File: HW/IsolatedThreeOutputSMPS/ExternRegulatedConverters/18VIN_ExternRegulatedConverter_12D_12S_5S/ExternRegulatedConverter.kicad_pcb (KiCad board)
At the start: 2 copper layers, 71.1 x 47 mm, 20 parts, among them J1 15VDC, J2 Conn_01x07, U1 RS6-1212D, U2 LM7805_TO220, U3 LM7812_TO220, U4 LM7912_TO220, U5 LM7812_TO220

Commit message: RevA layout PSU
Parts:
- added C10: 100nF, Capacitor_SMD:C_0805_2012Metric_Pad1.15x1.40mm_HandSolder, F.Cu at (104.9, 114.3)
- added C13: 1uF, Capacitor_SMD:CP_Elec_4x5.7, F.Cu at (154.2, 108.0)
- added C14: 4.7uF, Capacitor_SMD:CP_Elec_4x5.7, F.Cu at (150.4, 85.0)
- added D2: ES2G, Diode_SMD:D_SMA_Handsoldering, F.Cu at (154.2, 100.3)
- added HS2: Heatsink, Heatsink:Heatsink_SheetType_50x7mm_2Fixations, B.Cu at (108.0, 97.8)
- added REF**: MountingHole_3.2mm_M3_DIN965, MountingHole:MountingHole_3.2mm_M3_DIN965, F.Cu at (108.0, 91.1)
- added REF**: MountingHole_3.2mm_M3_DIN965, MountingHole:MountingHole_3.2mm_M3_DIN965, F.Cu at (108.0, 107.6)
- added REF**: MountingHole_3.2mm_M3_DIN965, MountingHole:MountingHole_3.2mm_M3_DIN965, F.Cu at (147.3, 91.1)
- added REF**: MountingHole_3.2mm_M3_DIN965, MountingHole:MountingHole_3.2mm_M3_DIN965, F.Cu at (147.3, 107.6)
- added REF**: MountingHole_3.2mm_M3_DIN965, MountingHole:MountingHole_3.2mm_M3_DIN965, F.Cu at (169.9, 75.2)
- added REF**: MountingHole_3.2mm_M3_DIN965, MountingHole:MountingHole_3.2mm_M3_DIN965, F.Cu at (169.9, 120.4)
- added REF**: MountingHole_3.2mm_M3_DIN965, MountingHole:MountingHole_3.2mm_M3_DIN965, F.Cu at (95.5, 120.4)
- added REF**: MountingHole_3.2mm_M3_DIN965, MountingHole:MountingHole_3.2mm_M3_DIN965, F.Cu at (95.5, 75.2)
- added U6: L7818CV, Package_TO_SOT_THT:TO-220-3_Vertical, B.Cu at (141.0, 91.4)
- added U7: L78M15ABV, Package_TO_SOT_THT:TO-220-3_Vertical, B.Cu at (141.0, 109.2)
- C1: value 2.2uF -> 4.7uF
- C12: renamed from C11; value 10uF -> 1uF
- C5: value 330nF -> 100nF; footprint Capacitor_SMD:C_0805_2012Metric_Pad1.15x1.40mm_HandSolder -> Capacitor_SMD:CP_Elec_4x5.7
- C6, C9: value 100nF -> 330nF
- C8: value 10uF -> 2.2uF
- D1: value D_Schottky -> BYS12-90-E3/TR
- HS1: value Heatsink -> Heatsink 6.8K/W
- J1: footprint Connector_Molex:Molex_KK-254_AE-6410-02A_1x02_P2.54mm_Vertical -> Connector_PinHeader_2.54mm:PinHeader_1x02_P2.54mm_Horizontal
- U1: value RS6-1212D -> ISE2409A-H; footprint ITX1212S:ITX1212S -> XPower_Converter_DCDC:ISE; moved to F.Cu
- U2: value LM7805_TO220 -> LM7812_TO220
- U3: value LM7812_TO220 -> LM7912_TO220
- U4: value LM7912_TO220 -> R2D-2415; footprint Package_TO_SOT_THT:TO-220-3_Vertical -> RS6:R2D; moved to F.Cu
- U5: value LM7812_TO220 -> LM7805_TO220
- moved C6 57.7 mm to (118.6, 118.9), turned to 270 degrees
- moved J1 57.3 mm to (164.5, 107.6)
- moved D1 55.6 mm to (167.0, 95.4)
- moved J2 51.3 mm to (98.8, 96.1)
- moved U5 46.7 mm to (114.3, 111.8), turned to 270 degrees
- moved C5 38.7 mm to (159.5, 116.7), turned to 0 degrees
- moved C1 30.8 mm to (97.9, 85.1), turned to 180 degrees
- moved C3 28.4 mm to (106.9, 85.1), turned to 180 degrees
- moved C12 28.2 mm to (105.4, 99.3), turned to 270 degrees
- moved U2 24.2 mm to (114.3, 85.1), turned to 270 degrees
- moved C11 19.7 mm to (109.9, 96.8), turned to 270 degrees
- moved C9 19.5 mm to (154.9, 94.5)
- moved C8 19.4 mm to (128.3, 97.8), turned to 180 degrees
- moved C2 19.3 mm to (156.0, 84.2)
- moved C4 15.5 mm to (121.9, 99.1), turned to 270 degrees
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- renumbered C10 to C11
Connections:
- C1 pad 1: +15V -> +24V
- C1 pad 2: GNDA -> GNDS
- C2 pad 1: +15V -> +24V
- C2 pad 2: GNDA -> GNDS
- C3 pad 1: Net-(C3-Pad1) -> +15V
- C3 pad 2: +15V -> +24V
- C4 pad 1: Net-(C4-Pad1) -> /-15V
- C4 pad 2: GNDA -> GNDS
- C5 pad 1: +15V -> /+18V
- C5 pad 2: GNDA -> GNDS
- C6 pad 1: +12P -> /+9V
- C6 pad 2: GNDA -> GNDS
- C7 pad 1: Net-(C3-Pad1) -> +15V
- C8 pad 2: Net-(C4-Pad1) -> /-15V
- C9 pad 1: +5V -> /+18V
- C9 pad 2: GNDA -> GNDS
- D1 pad 1: +15V -> +24V
- J1 pad 1: GNDA -> GNDS
- J2 pad 5: GNDA -> GNDS
- J2 pad 6: +12P -> +15V
- J2 pad 7: GNDA -> GNDS
- U1 pad 1: GNDA -> GNDS
- U1 pad 2: +15V -> +24V
- U1 pad 5: (no net) -> /+9V
- U1 pad 8: Net-(C4-Pad1) -> (no net)
- U2 pad 2: GNDA -> VCOM
- U2 pad 3: +5V -> +12V
- U3 pad 1: Net-(C3-Pad1) -> VCOM
- U3 pad 2: VCOM -> /-15V
- U3 pad 3: +12V -> -12V
- U4 pad 1: VCOM -> GNDS
- U4 pad 2: Net-(C4-Pad1) -> +24V
- U5 pad 1: +15V -> /+9V
- U5 pad 2: GNDA -> GNDS
- U5 pad 3: +12P -> +5V
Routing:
- net +24V: track 0.00 -> 114.1 mm
- net /+18V: track 0.00 -> 72.3 mm
- net Net-(C4-Pad1): track 65.7 -> 0.00 mm
- net Net-(C3-Pad1): track 58.0 -> 0.00 mm
- net +12P: track 57.7 -> 0.00 mm
- net VCOM: track 97.7 -> 57.2 mm
- net -12V: track 56.0 -> 16.8 mm
- net +5V: track 61.2 -> 26.2 mm
- net /-15V: track 0.00 -> 27.6 mm
- net +12V: track 48.1 -> 21.1 mm
- net +15V: track 126.5 -> 149.0 mm
- net /+9V: track 0.00 -> 14.3 mm
- net Net-(D1-Pad2): track 5.91 -> 9.56 mm
- net GNDS: track 0.00 -> 1.35 mm
- net GNDA: track 0.88 -> 0.00 mm
- added copper zone on F.Cu, net GNDS
- removed copper zone on F.Cu, net GNDA
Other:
- board size 71.1 x 47 mm -> 80 x 50.8 mm

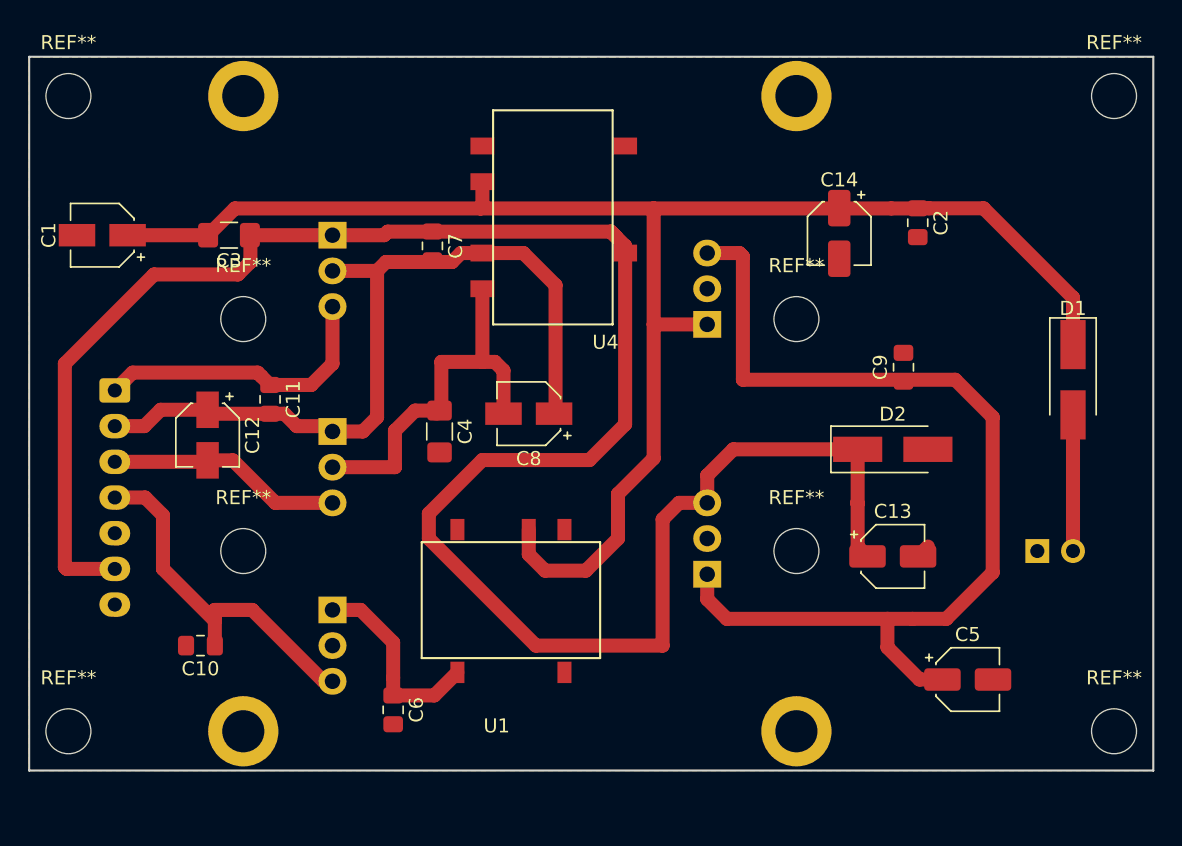
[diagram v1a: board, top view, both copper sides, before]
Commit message: updated RevA SMPS layout
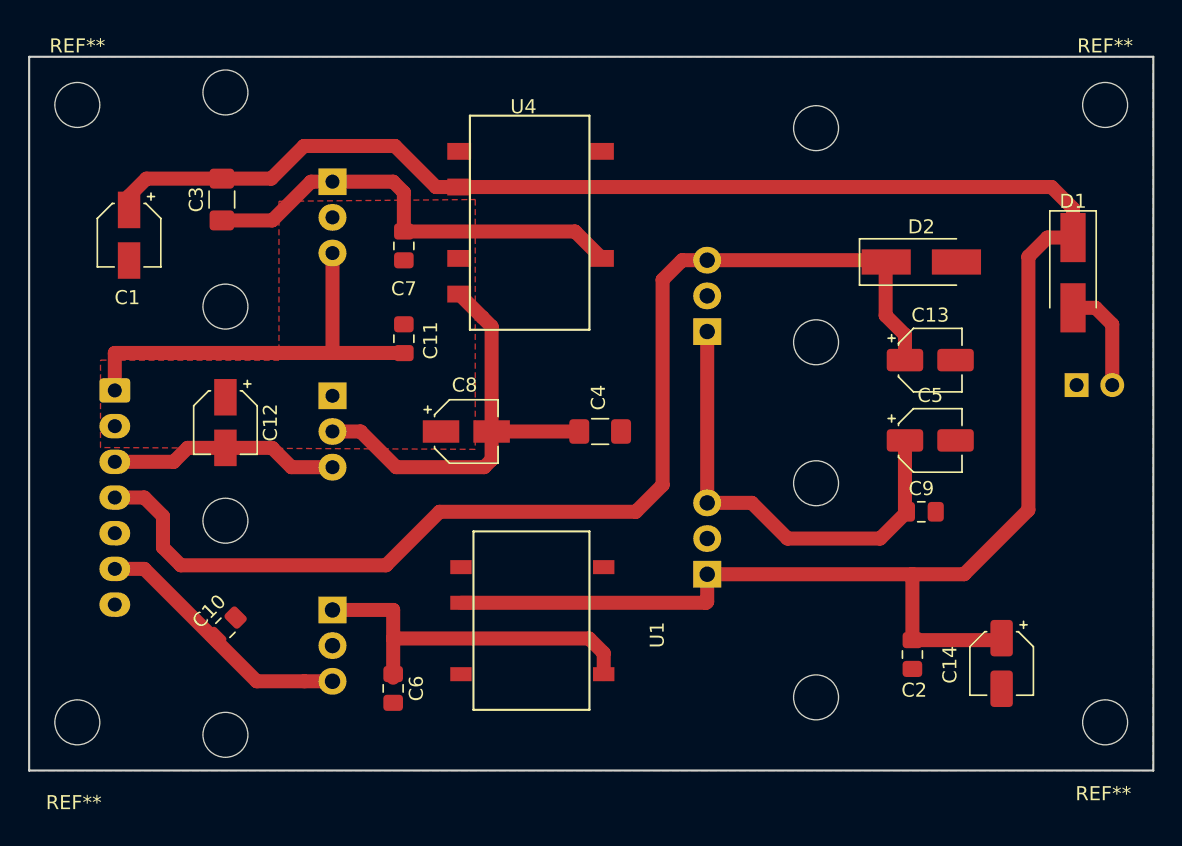
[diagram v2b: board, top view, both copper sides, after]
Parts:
- removed the HS1 at (147.3, 97.8)
- removed the REF** at (108.0, 91.1)
- removed the REF** at (108.0, 107.6)
- removed the REF** at (147.3, 91.1)
- removed the REF** at (147.3, 107.6)
- removed the REF** at (169.9, 75.2)
- removed the REF** at (169.9, 120.4)
- removed the REF** at (95.5, 120.4)
- removed the REF** at (95.5, 75.2)
- added HS2: SK 481/50 SA, FischerElektronikHeatsinks:SK481_SK480_25MM, B.Cu at (148.7, 110.4)
- added HS3: SK 481/50 SA, FischerElektronikHeatsinks:SK481_SK480_25MM, B.Cu at (148.7, 85.1)
- added REF**: MountingHole_3.2mm_M3, MountingHole:MountingHole_3.2mm_M3, F.Cu at (96.1, 75.8)
- added REF**: MountingHole_3.2mm_M3, MountingHole:MountingHole_3.2mm_M3, F.Cu at (96.1, 119.8)
- added REF**: MountingHole_3.2mm_M3, MountingHole:MountingHole_3.2mm_M3, F.Cu at (169.3, 119.8)
- added REF**: MountingHole_3.2mm_M3, MountingHole:MountingHole_3.2mm_M3, F.Cu at (169.3, 75.8)
- HS1: renamed from HS2; value Heatsink -> SK 480/50 SA; footprint Heatsink:Heatsink_SheetType_50x7mm_2Fixations -> FischerElektronikHeatsinks:SK512_SK480_50MM
- moved C14 32.7 mm to (161.9, 115.6)
- moved C2 30.7 mm to (155.6, 114.9)
- moved U6 17.8 mm to (141.0, 109.2)
- moved U7 17.3 mm to (141.0, 91.9)
- moved C5 17.2 mm to (156.8, 99.7)
- moved C13 14.2 mm to (156.8, 94.0)
- moved D2 13.5 mm to (156.2, 87.0)
- moved J1 12.1 mm to (167.3, 95.8)
- moved C4 11.4 mm to (133.3, 99.1), turned to 0 degrees
- moved C11 10.5 mm to (119.4, 92.5), turned to 90 degrees
- moved C9 10.4 mm to (156.2, 104.8), turned to 0 degrees
- moved D1 7.62 mm to (167.0, 87.8)
- moved U1 4.83 mm to (126.0, 108.7), turned to 270 degrees
- moved C8 4.62 mm to (123.8, 99.1), turned to 0 degrees
- moved U2 3.81 mm to (114.3, 81.3)
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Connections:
- net /-15V renamed /-15VA
- C3 pad 1: +15V -> /+15VA
- C7 pad 1: +15V -> /+15VA
- J2 pad 4: +5V -> +15V
- J2 pad 6: +15V -> +5V
- U2 pad 1: +15V -> /+15VA
- U4 pad 7: +15V -> /+15VA
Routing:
- net +15V: track 149.0 -> 83.6 mm
- net VCOM: track 57.2 -> 0.00 mm
- net /+18V: track 72.3 -> 33.4 mm
- net +24V: track 114.1 -> 150.7 mm
- net /+15VA: track 0.00 -> 32.1 mm
- net /+9V: track 14.3 -> 26.1 mm
- net +12V: track 21.1 -> 30.5 mm
- net +5V: track 26.2 -> 19.6 mm
- net /-15VA: track 27.6 -> 31.6 mm
- net Net-(D1-Pad2): track 9.56 -> 7.60 mm
- net GNDS: track 1.35 -> 0.36 mm
- added copper zone on F.Cu, net VCOM

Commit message: update
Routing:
- net +15V: track 83.6 -> 84.1 mm
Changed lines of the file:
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@@
     (thickness 1.6)
     (drawings 5)
-    (tracks 91)
+    (tracks 92)
     (zones 0)
     (modules 32)
@@
   )
   (setup
-    (last_trace_width 1)
+    (last_trace_width 0.25)
     (user_trace_width 1)
     (user_trace_width 1.5)
@@
     (add_net GNDS)
     (add_net "Net-(D1-Pad2)")
-    (add_net "Net-(U1-Pad8)")
-    (add_net "Net-(U4-Pad10)")
     (add_net VCOM)
   )
@@
   (gr_line (start 92.71 72.39) (end 172.72 72.39) (layer Edge.Cuts) (width 0.15))
   (segment (start 113.665 116.84) (end 114.3 116.84) (width 1) (layer F.Cu) (net 2))
-  (segment (start 98.933 104.14) (end 98.806 104.013) (width 1) (layer F.Cu) (net 6))
-  (segment (start 98.806 93.472) (end 114.3 93.472) (width 1) (layer F.Cu) (net 3))
-  (segment (start 98.806 96.139) (end 98.806 93.472) (width 1) (layer F.Cu) (net 3))
+  (segment (start 98.806 109.093) (end 98.933 109.22) (width 1) (layer F.Cu) (net 2))
+  (segment (start 112.3 116.84) (end 114.3 116.84) (width 1) (layer F.Cu) (net 2))
+  (segment (start 108.907 116.84) (end 112.3 116.84) (width 1) (layer F.Cu) (net 2))
+  (segment (start 100.906 108.839) (end 108.907 116.84) (width 1) (layer F.Cu) (net 2))
+  (segment (start 98.806 108.839) (end 100.906 108.839) (width 1) (layer F.Cu) (net 2))
   (segment (start 119.498 93.472) (end 119.507 93.481) (width 1) (layer F.Cu) (net 3))
   (segment (start 114.3 93.472) (end 119.498 93.472) (width 1) (layer F.Cu) (net 3))
   (segment (start 114.3 93.472) (end 114.3 86.36) (width 1) (layer F.Cu) (net 3))
+  (segment (start 98.806 93.98) (end 113.792 93.98) (width 1) (layer F.Cu) (net 3))
+  (segment (start 113.792 93.98) (end 114.3 93.472) (width 1) (layer F.Cu) (net 3))
+  (segment (start 98.806 96.139) (end 98.806 93.98) (width 1) (layer F.Cu) (net 3))
   (segment (start 103.991 100.225) (end 106.68 100.225) (width 1) (layer F.Cu) (net 4))
   (segment (start 102.997 101.219) (end 103.991 100.225) (width 1) (layer F.Cu) (net 4))
@@
   (segment (start 168.616 90.257) (end 167.005 90.257) (width 1) (layer F.Cu) (net 5))
   (segment (start 169.799 95.758) (end 169.799 91.44) (width 1) (layer F.Cu) (net 5))
-  (segment (start 98.806 109.093) (end 98.933 109.22) (width 1) (layer F.Cu) (net 2))
-  (segment (start 112.3 116.84) (end 114.3 116.84) (width 1) (layer F.Cu) (net 2))
-  (segment (start 108.907 116.84) (end 112.3 116.84) (width 1) (layer F.Cu) (net 2))
-  (segment (start 100.906 108.839) (end 108.907 116.84) (width 1) (layer F.Cu) (net 2))
-  (segment (start 98.806 108.839) (end 100.906 108.839) (width 1) (layer F.Cu) (net 2))
+  (segment (start 98.933 104.14) (end 98.806 104.013) (width 1) (layer F.Cu) (net 6))
   (segment (start 153.583 86.868) (end 153.71 86.995) (width 1) (layer F.Cu) (net 6))
   (segment (start 140.97 86.868) (end 153.583 86.868) (width 1) (layer F.Cu) (net 6))
@@
   (segment (start 155.045 93.98) (end 155.045 92.18) (width 1) (layer F.Cu) (net 6))
   (segment (start 139.192 86.868) (end 140.97 86.868) (width 1) (layer F.Cu) (net 6))
-  (segment (start 102.235 107.315) (end 103.505 108.585) (width 1) (layer F.Cu) (net 6))
+  (segment (start 137.795 102.87) (end 137.795 88.265) (width 1) (layer F.Cu) (net 6))
+  (segment (start 135.89 104.775) (end 137.795 102.87) (width 1) (layer F.Cu) (net 6))
+  (segment (start 117.475 109.22) (end 121.92 104.775) (width 1) (layer F.Cu) (net 6))
+  (segment (start 137.795 88.265) (end 139.192 86.868) (width 1) (layer F.Cu) (net 6))
   (segment (start 102.235 105.088) (end 102.235 107.315) (width 1) (layer F.Cu) (net 6))
+  (segment (start 102.235 107.315) (end 104.14 109.22) (width 1) (layer F.Cu) (net 6))
+  (segment (start 104.14 109.22) (end 117.475 109.22) (width 1) (layer F.Cu) (net 6))
   (segment (start 100.906 103.759) (end 102.235 105.088) (width 1) (layer F.Cu) (net 6))
-  (segment (start 137.795 88.265) (end 139.192 86.868) (width 1) (layer F.Cu) (net 6))
-  (segment (start 137.795 102.87) (end 137.795 88.265) (width 1) (layer F.Cu) (net 6))
-  (segment (start 103.505 108.585) (end 118.11 108.585) (width 1) (layer F.Cu) (net 6))
-  (segment (start 135.89 104.775) (end 137.795 102.87) (width 1) (layer F.Cu) (net 6))
   (segment (start 121.92 104.775) (end 135.89 104.775) (width 1) (layer F.Cu) (net 6))
-  (segment (start 118.11 108.585) (end 121.92 104.775) (width 1) (layer F.Cu) (net 6))
   (segment (start 98.806 103.759) (end 100.906 103.759) (width 1) (layer F.Cu) (net 6))
   (segment (start 106.426 81.0625) (end 101.0555 81.0625) (width 1) (layer F.Cu) (net 7))

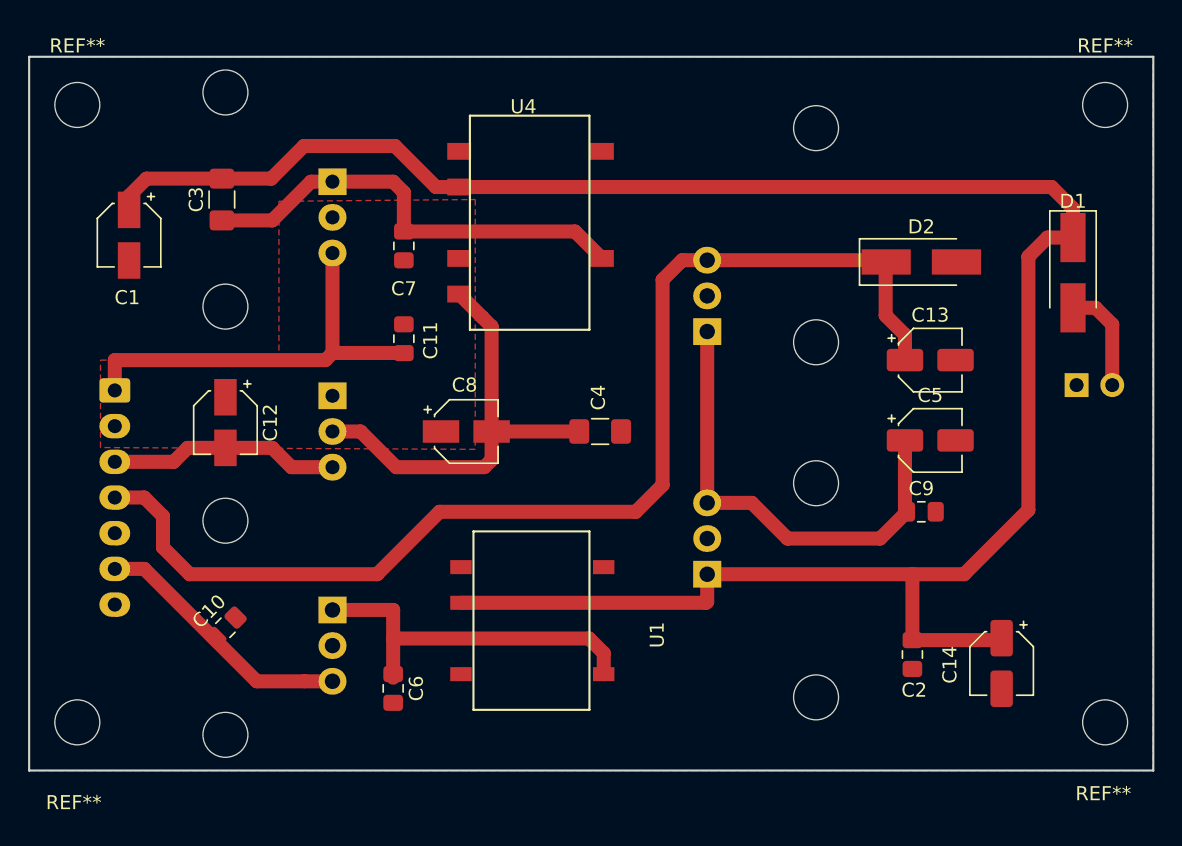
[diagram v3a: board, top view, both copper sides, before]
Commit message: updated layout
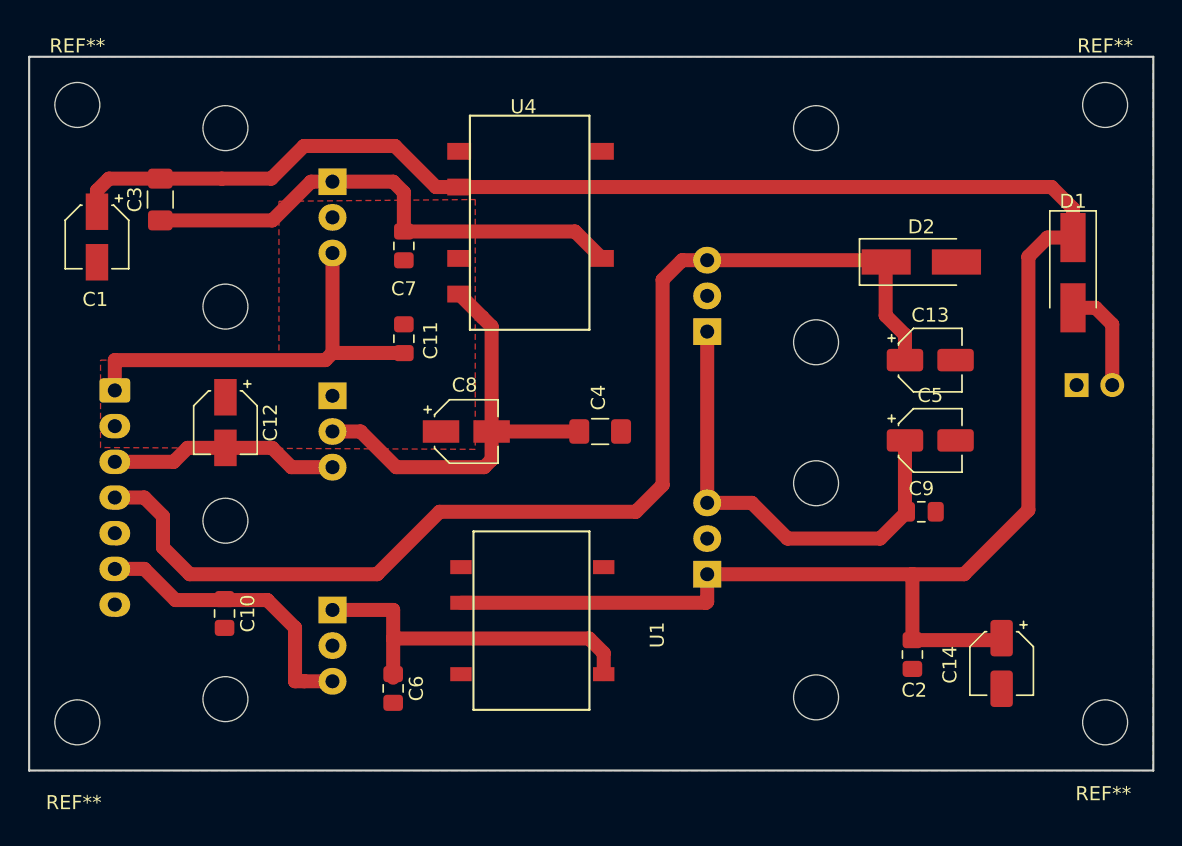
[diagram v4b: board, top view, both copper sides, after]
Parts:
- moved C3 4.38 mm to (102.0, 82.5)
- moved C1 2.29 mm to (97.5, 85.2)
- moved C10 1.02 mm to (106.6, 112.0), turned to 270 degrees
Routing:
- net /+15VA: track 32.1 -> 36.5 mm
- net +24V: track 150.7 -> 153.3 mm
- net +5V: track 19.6 -> 21.9 mm
